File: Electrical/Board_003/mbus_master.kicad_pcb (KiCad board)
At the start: 2 copper layers, 30 x 25 mm, 14 parts, among them J1 Conn_01x02, J2 Conn_01x02, J3 Conn_01x02, Q1 BC337, Q2 BC337, Q3 BC337, Q4 BD136

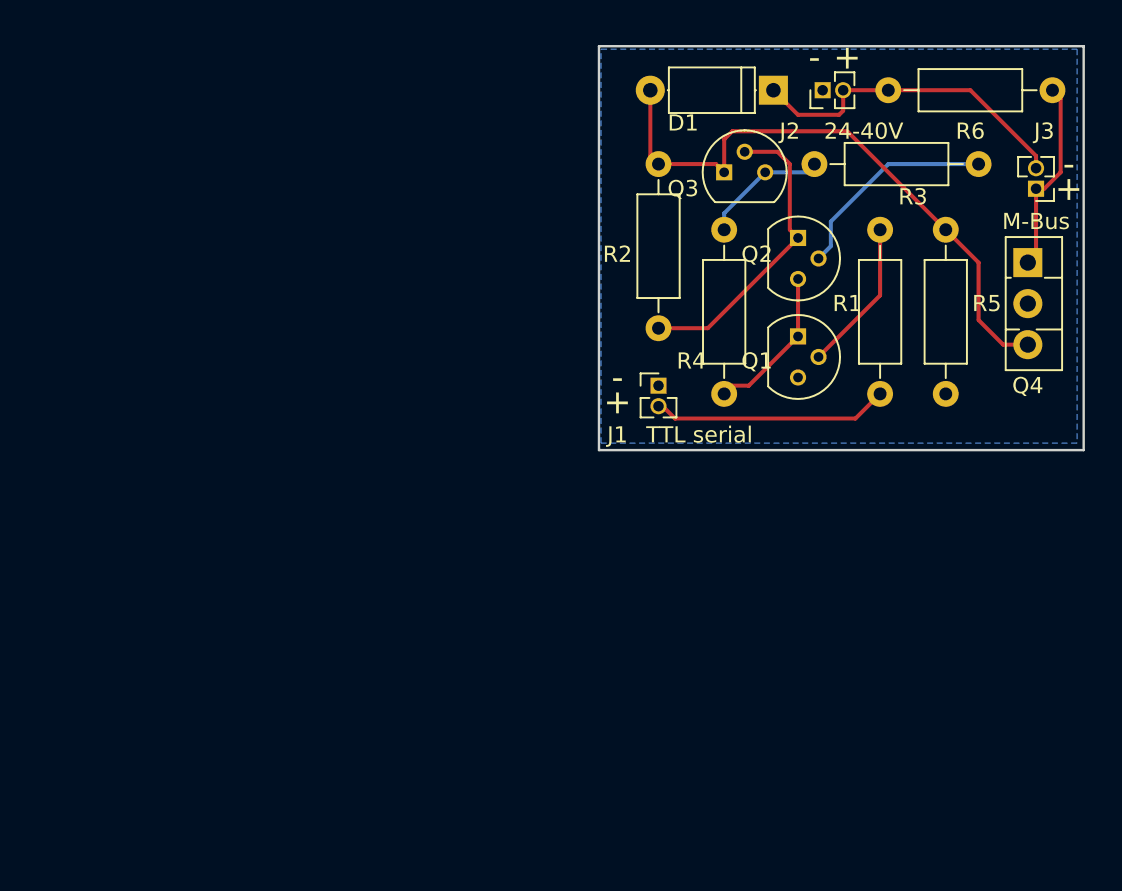
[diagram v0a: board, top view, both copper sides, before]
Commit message: Update schematic and pcb to match mbus_master_101
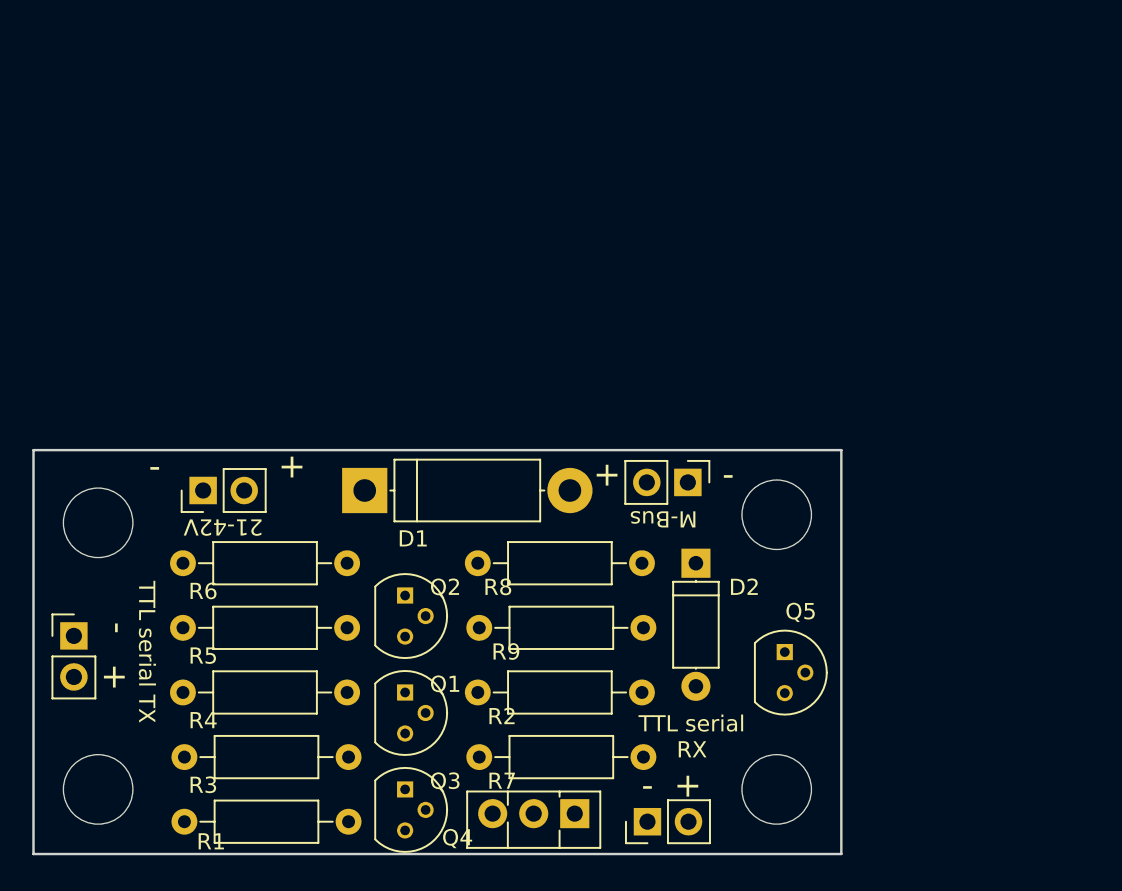
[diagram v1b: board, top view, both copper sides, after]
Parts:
- added D2: 4.7V, Diodes_THT:D_A-405_P7.62mm_Horizontal, F.Cu at (141.0, 107.0)
- added J4: Conn_01x02, Pin_Headers:Pin_Header_Straight_1x02_Pitch2.54mm, F.Cu at (138.0, 123.0)
- added MK1: Mounting_Hole, Mounting_Holes:MountingHole_4.3mm_M4_ISO14580, F.Cu at (104.0, 121.0)
- added MK2: Mounting_Hole, Mounting_Holes:MountingHole_4.3mm_M4_ISO14580, F.Cu at (146.0, 121.0)
- added MK3: Mounting_Hole, Mounting_Holes:MountingHole_4.3mm_M4_ISO14580, F.Cu at (146.0, 104.0)
- added MK4: Mounting_Hole, Mounting_Holes:MountingHole_4.3mm_M4_ISO14580, F.Cu at (104.0, 104.5)
- added Q5: BC337, TO_SOT_Packages_THT:TO-92_Molded_Narrow, F.Cu at (146.5, 112.5)
- added R7: 82, Resistors_THT:R_Axial_DIN0207_L6.3mm_D2.5mm_P10.16mm_Horizontal, F.Cu at (137.8, 119.0)
- added R8: 10k, Resistors_THT:R_Axial_DIN0207_L6.3mm_D2.5mm_P10.16mm_Horizontal, F.Cu at (127.5, 107.0)
- added R9: 1k, Resistors_THT:R_Axial_DIN0207_L6.3mm_D2.5mm_P10.16mm_Horizontal, F.Cu at (137.8, 111.0)
- D1: value D_Zener_Small_ALT -> 13V; footprint Diodes_THT:D_A-405_P7.62mm_Horizontal -> Diodes_THT:D_5W_P12.70mm_Horizontal
- J1, J2, J3: footprint Pin_Headers:Pin_Header_Straight_1x02_Pitch1.27mm -> Pin_Headers:Pin_Header_Straight_1x02_Pitch2.54mm
- R1: value 1k -> 10k
- R2: value 6k8 -> 8.2k
- R3: value 1 -> 10k
- R4: value 150 -> 10k
- R5: value 22k -> 10k
- moved R5 53.3 mm to (109.2, 111.0), turned to 0 degrees
- moved R6 52.6 mm to (109.2, 107.0)
- moved R1 49.2 mm to (119.5, 123.0), turned to 180 degrees
- moved R3 46.7 mm to (119.5, 119.0), turned to 180 degrees
- moved J2 45.7 mm to (110.5, 102.5)
- moved Q4 44.2 mm to (133.5, 122.5), turned to 180 degrees
- moved R4 44.1 mm to (109.2, 115.0), turned to 0 degrees
- moved Q3 43.0 mm to (123.0, 121.0), turned to 270 degrees
- moved J1 39.4 mm to (102.5, 111.5)
- moved D1 35.4 mm to (120.5, 102.5), turned to 0 degrees
- moved R2 34.6 mm to (127.5, 115.0), turned to 0 degrees
- moved Q2 32.9 mm to (123.0, 109.0)
- moved Q1 32.8 mm to (123.0, 115.0)
- moved J3 28.2 mm to (140.5, 102.0), turned to 270 degrees
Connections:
- Q2 pad 2: Net-(Q2-Pad2) -> Net-(Q1-Pad1)
- Q2 pad 3: Net-(Q1-Pad1) -> Net-(D1-Pad2)
- Q3 pad 1: Net-(D1-Pad2) -> Net-(Q3-Pad1)
- Q3 pad 2: Net-(Q2-Pad1) -> Net-(Q3-Pad2)
- Q3 pad 3: Net-(Q3-Pad3) -> GND
- Q4 pad 2: GND -> Net-(Q4-Pad2)
- R1 pad 1: Net-(Q1-Pad2) -> Net-(Q3-Pad2)
- R2 pad 2: Net-(Q2-Pad1) -> Net-(Q3-Pad1)
- R3 pad 1: Net-(Q3-Pad3) -> Net-(Q1-Pad2)
- R3 pad 2: Net-(Q2-Pad2) -> Net-(J1-Pad2)
- R4 pad 1: Net-(Q3-Pad3) -> /EXT_PWR
- R5 pad 1: Net-(D1-Pad2) -> /EXT_PWR
- R5 pad 2: GND -> Net-(Q2-Pad1)
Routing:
- net Net-(D1-Pad2): track 37.6 -> 0.00 mm
- net /EXT_PWR: track 20.7 -> 0.00 mm
- net Net-(Q2-Pad1): track 18.8 -> 0.00 mm
- net Net-(J1-Pad2): track 14.7 -> 0.00 mm
- net Net-(Q2-Pad2): track 13.2 -> 0.00 mm
- net /MBus-: track 12.0 -> 0.00 mm
- net Net-(Q1-Pad1): track 9.60 -> 0.00 mm
- net Net-(Q1-Pad2): track 9.45 -> 0.00 mm
- net Net-(Q3-Pad3): track 7.87 -> 0.00 mm
- removed copper zone on B.Cu, net GND
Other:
- board size 30 x 25 mm -> 50 x 25 mm
- board text added: "21-42V"
- board text added: "M-Bus master Rev B 2018"
- board text added: "TTL serial RX"
- board text added: "TTL serial TX"
- board text removed: "24-40V"
- board text removed: "M-Bus simulator transmit only Rev A 2018"
- board text removed: "TTL serial"

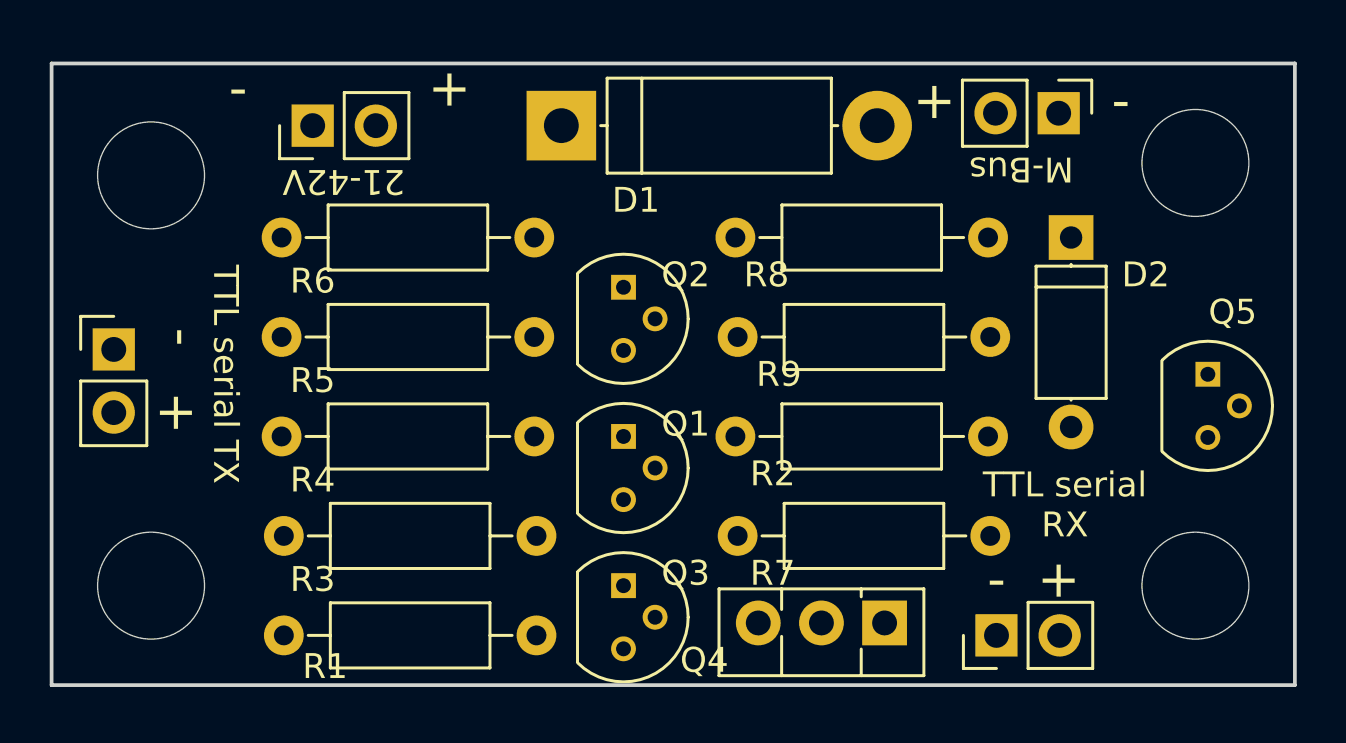
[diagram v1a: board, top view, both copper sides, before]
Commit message: Via stiching
Tip from http://www.youtube.com/watch?v=Hp5ngKtl7S4
Via Stitching In KiCad (without traces)
By Contextual Electronics
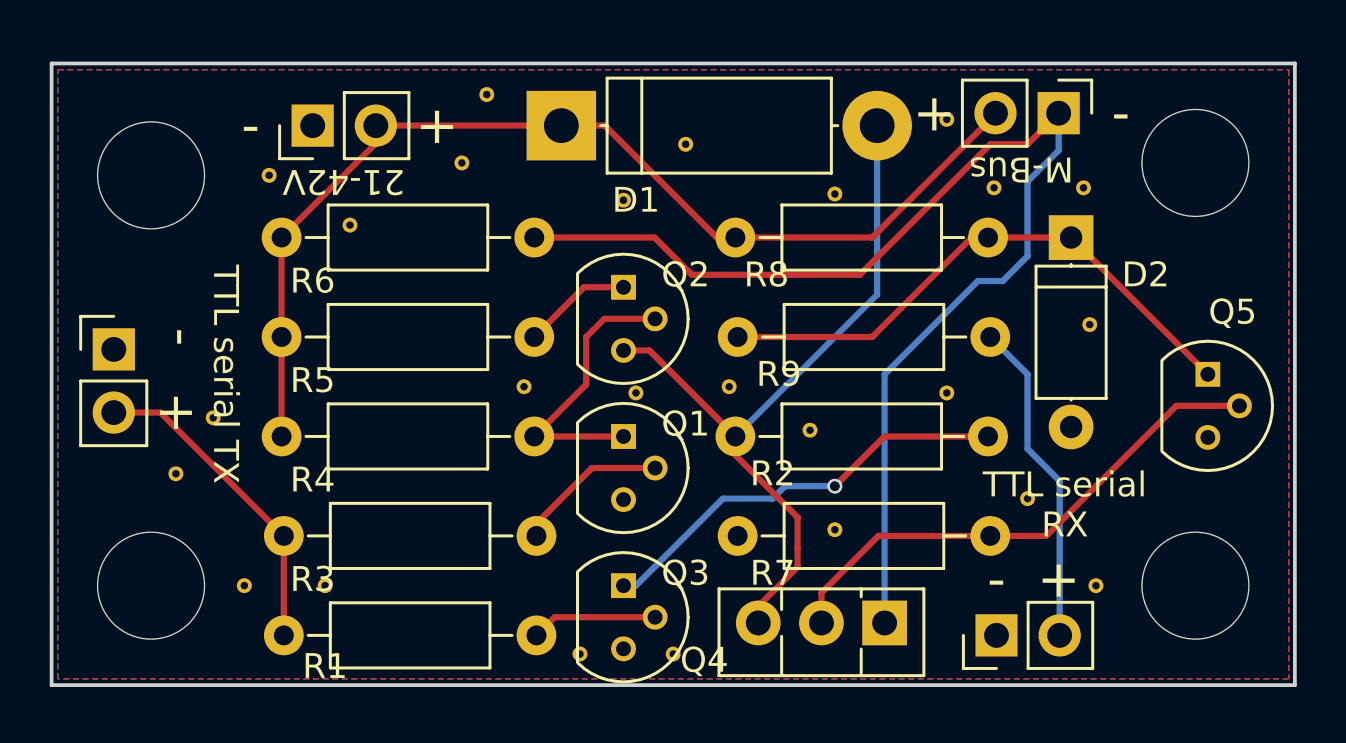
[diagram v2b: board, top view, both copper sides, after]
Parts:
- added REF**: VIA-0.6mm, AmsToMqttBridge:VIA-0.6mm, F.Cu at (125.5, 103.2)
- added REF**: VIA-0.6mm, AmsToMqttBridge:VIA-0.6mm, F.Cu at (139.2, 117.5)
- added REF**: VIA-0.6mm, AmsToMqttBridge:VIA-0.6mm, F.Cu at (125.0, 123.8)
- added REF**: VIA-0.6mm, AmsToMqttBridge:VIA-0.6mm, F.Cu at (121.2, 123.8)
- added REF**: VIA-0.6mm, AmsToMqttBridge:VIA-0.6mm, F.Cu at (123.5, 113.2)
- added REF**: VIA-0.6mm, AmsToMqttBridge:VIA-0.6mm, F.Cu at (106.5, 114.2)
- added REF**: VIA-0.6mm, AmsToMqttBridge:VIA-0.6mm, F.Cu at (105.0, 116.5)
- added REF**: VIA-0.6mm, AmsToMqttBridge:VIA-0.6mm, F.Cu at (111.0, 121.0)
- added REF**: VIA-0.6mm, AmsToMqttBridge:VIA-0.6mm, F.Cu at (107.8, 121.0)
- added REF**: VIA-0.6mm, AmsToMqttBridge:VIA-0.6mm, F.Cu at (108.8, 104.5)
- added REF**: VIA-0.6mm, AmsToMqttBridge:VIA-0.6mm, F.Cu at (112.0, 106.5)
- added REF**: VIA-0.6mm, AmsToMqttBridge:VIA-0.6mm, F.Cu at (117.5, 101.2)
- added REF**: VIA-0.6mm, AmsToMqttBridge:VIA-0.6mm, F.Cu at (127.2, 113.0)
- added REF**: VIA-0.6mm, AmsToMqttBridge:VIA-0.6mm, F.Cu at (123.0, 105.5)
- added REF**: VIA-0.6mm, AmsToMqttBridge:VIA-0.6mm, F.Cu at (141.8, 110.5)
- added REF**: VIA-0.6mm, AmsToMqttBridge:VIA-0.6mm, F.Cu at (141.5, 105.0)
- added REF**: VIA-0.6mm, AmsToMqttBridge:VIA-0.6mm, F.Cu at (136.0, 102.2)
- added REF**: VIA-0.6mm, AmsToMqttBridge:VIA-0.6mm, F.Cu at (131.5, 105.2)
- added REF**: VIA-0.6mm, AmsToMqttBridge:VIA-0.6mm, F.Cu at (116.5, 104.0)
- added REF**: VIA-0.6mm, AmsToMqttBridge:VIA-0.6mm, F.Cu at (119.0, 113.0)
- added REF**: VIA-0.6mm, AmsToMqttBridge:VIA-0.6mm, F.Cu at (130.5, 114.8)
- added REF**: VIA-0.6mm, AmsToMqttBridge:VIA-0.6mm, F.Cu at (131.5, 118.8)
- added REF**: VIA-0.6mm, AmsToMqttBridge:VIA-0.6mm, F.Cu at (136.0, 113.2)
- added REF**: VIA-0.6mm, AmsToMqttBridge:VIA-0.6mm, F.Cu at (137.9, 105.0)
- added REF**: VIA-0.6mm, AmsToMqttBridge:VIA-0.6mm, F.Cu at (142.0, 121.0)
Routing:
- net /MBus-: track 0.00 -> 48.4 mm
- net /EXT_PWR: track 0.00 -> 43.0 mm
- net Net-(D1-Pad2): track 0.00 -> 30.0 mm
- net Net-(D2-Pad1): track 0.00 -> 22.8 mm
- net Net-(Q4-Pad2): track 0.00 -> 21.1 mm
- net Net-(Q3-Pad1): track 0.00 -> 17.1 mm, vias 0 -> 1
- net Net-(J4-Pad2): track 0.00 -> 13.2 mm
- net Net-(J1-Pad2): track 0.00 -> 12.9 mm
- net Net-(Q1-Pad1): track 0.00 -> 11.5 mm
- net Net-(Q1-Pad2): track 0.00 -> 6.19 mm
- net Net-(Q3-Pad2): track 0.00 -> 5.07 mm
- net Net-(Q2-Pad1): track 0.00 -> 4.42 mm
- added copper zone on B.Cu, net GND
- added copper zone on F.Cu, net GND
